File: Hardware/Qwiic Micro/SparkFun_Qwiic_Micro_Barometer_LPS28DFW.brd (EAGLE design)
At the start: 7.6 x 19.1 mm, 38 parts, among them J2 QWIIC_RIGHT_ANGLE, U1 LPS28DFW

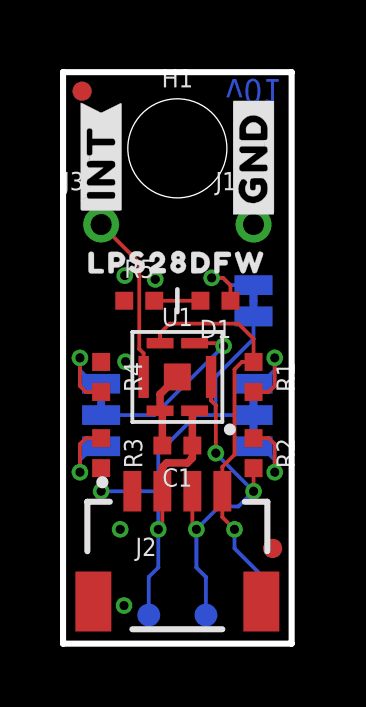
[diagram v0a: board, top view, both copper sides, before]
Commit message: Design review updates
Both:
Bump version number to v10
Change LPS28DF section name to "Barometer - LPS28DFW" in schematics
Remove SPI from ADR jumper in schematics
Add ordering instructions to boards

1x1:
Make SCL and SDA traces not overlap near Qwiic connector
Move OSHW down between connector and standoff
Move I@C jumper up to give more GND pour under sensor
Add SparkFun logo to bottom silk

Micro:
Space out test points in schematic
Add text about 22 AWG wires in schematic
Move OSHW logo up slightly to not clip at test points
Flip ADR labels to be correct
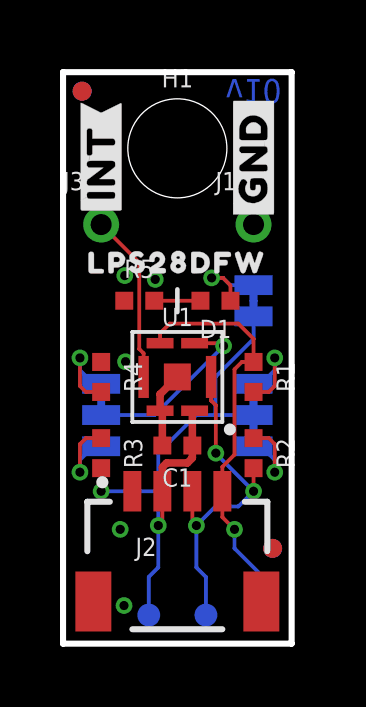
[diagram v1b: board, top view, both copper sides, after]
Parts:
- added U$19: (no value), SparkFun-Aesthetics:ORDERING_INSTRUCTIONS
- moved U$16 2.79 mm to (1.27, 6.22)
- moved U$17 2.79 mm to (1.27, 9.02)
- moved LOGO1 0.13 mm to (3.81, 2.67)
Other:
- board text added: "1.6mm Thickness"
- board text added: "2-Layer"
- board text added: "Lead-Free HASL"
- board text added: "v10"
- board text removed: "v01"
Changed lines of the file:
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@@
 <text x="-17.78" y="-2.54" size="1.778" layer="47" font="vector" ratio="15">Units: inches</text>
 <text x="7.62" y="-13.97" size="1.778" layer="51" font="vector">Dryw Wade</text>
-<text x="6.35" y="18.415" size="0.8128" layer="16" font="vector" ratio="20" rot="SMR180" align="center">v01</text>
+<text x="6.35" y="18.415" size="0.8128" layer="16" font="vector" ratio="20" rot="SMR180" align="center">v10</text>
 <dimension x1="0" y1="0" x2="7.62" y2="0" x3="3.81" y3="-3.81" textsize="1.778" textratio="15" layer="47" unit="inch"/>
 <dimension x1="0" y1="0" x2="0" y2="13.97" x3="-1.27" y3="6.985" textsize="1.778" textratio="15" layer="47" unit="inch"/>
@@
 <dimension x1="0" y1="19.05" x2="3.81" y2="19.05" x3="1.905" y3="24.13" textsize="1.778" textratio="15" layer="47" unit="inch"/>
 <dimension x1="0" y1="19.05" x2="1.27" y2="19.05" x3="0.635" y3="27.94" textsize="1.778" textratio="15" layer="47" unit="inch"/>
+<text x="17.78" y="38.1" size="2.54" layer="51" font="vector">2-Layer</text>
+<text x="17.78" y="34.29" size="2.54" layer="51" font="vector">1.6mm Thickness</text>
+<text x="17.78" y="30.48" size="2.54" layer="51" font="vector">Lead-Free HASL</text>
 </plain>
 <attributes>
@@
 <attribute name="VALUE" x="2.159" y="1.778" size="0.6096" layer="27" font="vector" ratio="20"/>
 </element>
-<element name="LOGO1" library="SparkFun-Aesthetics" package="OSHW-LOGO-S" value="OSHW-LOGOS" x="3.81" y="2.54" smashed="yes" rot="MR0"/>
+<element name="LOGO1" library="SparkFun-Aesthetics" package="OSHW-LOGO-S" value="OSHW-LOGOS" x="3.81" y="2.667" smashed="yes" rot="MR0"/>
 <element name="LOGO2" library="SparkFun-Aesthetics" package="QWIIC_3MM" value="QWIIC_LOGO_3MM" x="3.81" y="5.08" smashed="yes" rot="MR0"/>
 <element name="LOGO3" library="SparkFun-Aesthetics" package="BLANK" value="SFE_LOGO_NAME_FLAMEBLANK" x="-19.05" y="-16.51" smashed="yes"/>
@@
 <element name="U$10" library="output" package="#ADR#0" value="" x="2.794" y="7.62" smashed="yes" rot="MR90"/>
 <element name="U$13" library="output" package="#PWR#0" value="" x="5.588" y="11.43" smashed="yes" rot="MR0"/>
-<element name="U$16" library="output" package="#0X5D#0" value="" x="1.27" y="9.017" smashed="yes" rot="MR90"/>
-<element name="U$17" library="output" package="#0X5C#0" value="" x="1.27" y="6.223" smashed="yes" rot="MR90"/>
+<element name="U$16" library="output" package="#0X5D#0" value="" x="1.27" y="6.223" smashed="yes" rot="MR90"/>
+<element name="U$17" library="output" package="#0X5C#0" value="" x="1.27" y="9.017" smashed="yes" rot="MR90"/>
 <element name="TP1" library="SparkFun-Connectors" package="PAD.03X.03" value="TEST-POINT3" x="0.9525" y="0.9525" smashed="yes" rot="MR90"/>
 <element name="TP2" library="SparkFun-Connectors" package="PAD.03X.03" value="TEST-POINT3" x="2.8575" y="0.9525" smashed="yes" rot="MR90"/>
@@
 <element name="U$5" library="output" package="LPS28DFW0" value="" x="3.81" y="12.7" smashed="yes"/>
 <element name="U$6" library="SparkFun-Aesthetics" package="SFE_LOGO_FLAME_.1" value="" x="3.81" y="13.335" smashed="yes" rot="MR0"/>
+<element name="U$19" library="SparkFun-Aesthetics" package="ORDERING_INSTRUCTIONS" value="" x="16.51" y="50.8" smashed="yes"/>
 </elements>
 <signals>
@@
 <contactref element="PWR" pad="2"/>
 <contactref element="TP2" pad="1"/>
-<wire x1="3.31" y1="5.08" x2="3.31" y2="3.945" width="0.127" layer="1"/>
-<wire x1="3.31" y1="3.945" x2="3.175" y2="3.81" width="0.127" layer="1"/>
-<via x="3.175" y="3.81" extent="1-16" drill="0.3048"/>
-<wire x1="3.175" y1="3.81" x2="3.175" y2="2.54" width="0.127" layer="16"/>
+<wire x1="3.31" y1="5.08" x2="3.31" y2="4.072" width="0.127" layer="1"/>
+<wire x1="3.31" y1="4.072" x2="3.175" y2="3.937" width="0.127" layer="1"/>
+<via x="3.175" y="3.937" extent="1-16" drill="0.3048"/>
+<wire x1="3.175" y1="3.937" x2="3.175" y2="2.54" width="0.127" layer="16"/>
 <wire x1="3.175" y1="2.54" x2="2.8575" y2="2.2225" width="0.127" layer="16"/>
 <wire x1="2.8575" y1="2.2225" x2="2.8575" y2="0.9525" width="0.127" layer="16"/>
@@
 <wire x1="5.08" y1="8.89" x2="6.35" y2="10.16" width="0.127" layer="16"/>
 <wire x1="6.35" y1="10.16" x2="6.35" y2="10.9093" width="0.127" layer="16"/>
-<wire x1="3.175" y1="3.81" x2="3.175" y2="5.08" width="0.127" layer="16"/>
+<wire x1="3.175" y1="3.937" x2="3.175" y2="5.08" width="0.127" layer="16"/>
 <wire x1="3.175" y1="5.08" x2="3.175" y2="6.35" width="0.127" layer="16"/>
 <wire x1="1.27" y1="5.08" x2="3.175" y2="5.08" width="0.127" layer="16"/>
@@
 <contactref element="R2" pad="2"/>
 <contactref element="TP3" pad="1"/>
-<wire x1="4.31" y1="5.08" x2="4.31" y2="3.945" width="0.127" layer="1"/>
-<wire x1="4.31" y1="3.945" x2="4.445" y2="3.81" width="0.127" layer="1"/>
-<via x="4.445" y="3.81" extent="1-16" drill="0.3048"/>
-<wire x1="4.445" y1="3.81" x2="4.445" y2="2.54" width="0.127" layer="16"/>
+<wire x1="4.31" y1="5.08" x2="4.31" y2="4.072" width="0.127" layer="1"/>
+<wire x1="4.31" y1="4.072" x2="4.445" y2="3.937" width="0.127" layer="1"/>
+<via x="4.445" y="3.937" extent="1-16" drill="0.3048"/>
+<wire x1="4.445" y1="3.937" x2="4.445" y2="2.54" width="0.127" layer="16"/>
 <wire x1="4.7625" y1="2.2225" x2="4.7625" y2="0.9525" width="0.127" layer="16"/>
 <wire x1="4.7625" y1="2.2225" x2="4.445" y2="2.54" width="0.127" layer="16"/>
-<wire x1="4.445" y1="3.81" x2="5.207" y2="4.572" width="0.127" layer="16"/>
-<wire x1="5.842" y1="4.572" x2="5.207" y2="4.572" width="0.127" layer="16"/>
+<wire x1="4.445" y1="3.937" x2="5.08" y2="4.572" width="0.127" layer="16"/>
+<wire x1="5.842" y1="4.572" x2="5.08" y2="4.572" width="0.127" layer="16"/>
 <wire x1="5.842" y1="4.572" x2="6.35" y2="5.08" width="0.127" layer="16"/>
 <via x="6.35" y="5.08" extent="1-16" drill="0.3048"/>

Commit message: Remove library file
Part is in SFE Eagle library, update part in design
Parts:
- U1: device LPS28DFW:LPS28DFW -> SparkFun-Sensors:CCLGA-7L
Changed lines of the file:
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@@
 <element name="LOGO2" library="SparkFun-Aesthetics" package="QWIIC_3MM" value="QWIIC_LOGO_3MM" x="3.81" y="5.08" smashed="yes" rot="MR0"/>
 <element name="LOGO3" library="SparkFun-Aesthetics" package="BLANK" value="SFE_LOGO_NAME_FLAMEBLANK" x="-19.05" y="-16.51" smashed="yes"/>
-<element name="U1" library="LPS28DFW" package="LPS28DFW" value="LPS28DFW" x="3.81" y="8.89" smashed="yes">
+<element name="U1" library="SparkFun-Sensors" package="CCLGA-7L" value="LPS28DFW" x="3.81" y="8.89" smashed="yes">
 <attribute name="NAME" x="3.81" y="10.89" size="0.6096" layer="25" font="vector" ratio="20" align="center"/>
 <attribute name="PROD_ID" value="IC-17197" x="3.81" y="8.89" size="1.778" layer="27" display="off"/>
